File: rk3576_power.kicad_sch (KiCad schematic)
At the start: 30 parts, among them U27 RK3576

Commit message: Add files via upload
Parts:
- C63: renamed from C398; value 100n -> 1u
- C64: renamed from C259; value 100n -> 1u
- C65: renamed from C266; value 100n -> 1u
- C74: renamed from C419; value 100n -> 1u
- C75: renamed from C408; value 100n -> 1u
- C76: renamed from C409; value 100n -> 1u
- C83: renamed from C423; value 100n -> 1u
- C84: renamed from C424; value 100n -> 1u
- C85: renamed from C417; value 100n -> 1u
- renumbered C407 to C60, C402 to C61, C399 to C62, C267 to C66, C268 to C67, C270 to C68, C271 to C69, C272 to C70, C273 to C71, C416 to C72, C418 to C73, C410 to C77, C411 to C78, C412 to C79, C413 to C80, C414 to C81, C415 to C82, C420 to C86, C421 to C87, C422 to C88, U27 to U2

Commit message: SBC Board V0.2
The SBC schematics before footprint and part number check
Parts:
- U3: renamed from U2; footprint (none) -> easyeda2kicad:FCCSP-698_L17.2-W16.1-TL_RK3576
- renumbered C60 to C67, C61 to C68, C62 to C69, C63 to C70, C64 to C71, C65 to C72, C66 to C73, C67 to C74, C68 to C75, C69 to C76, C70 to C77, C71 to C78, C72 to C79, C73 to C80, C74 to C81, C75 to C82, C76 to C83, C77 to C84, C78 to C85, C79 to C86, C80 to C87, C81 to C88, C82 to C89, C83 to C90, C84 to C91, C85 to C92, C86 to C93, C87 to C94, C88 to C95

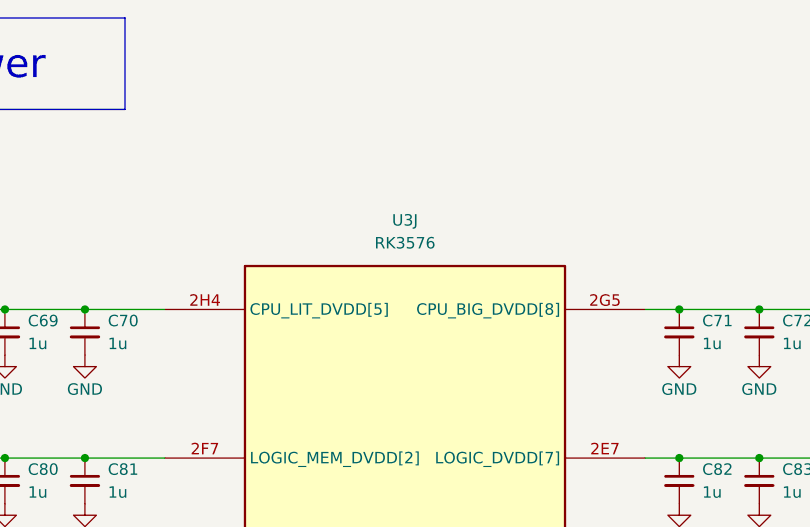
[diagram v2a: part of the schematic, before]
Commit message: SBCv0.3
there is no big thing update just some LCSC & Mouser parts
and Big problem deleted alot of component values (:
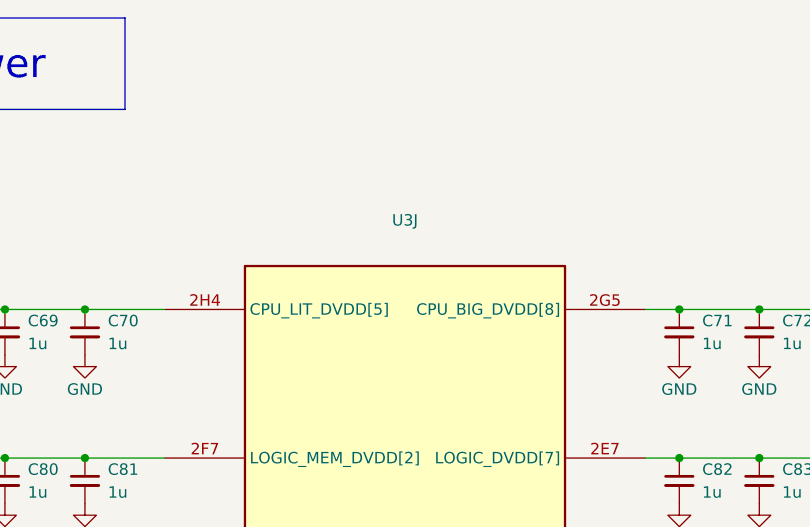
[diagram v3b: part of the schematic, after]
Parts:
- C67, C77, C78, C79, C86, C87, C95: footprint Capacitor_SMD:C_0402_1005Metric_Pad0.74x0.62mm_HandSolder -> Capacitor_SMD:C_0603_1608Metric; LCSC Part (none) -> C19702; Mouser Part (none) -> 187-CL10A106KP8NNNC
- C68, C69, C70, C71, C72, C73, C74, C75, C76, C80, C81, C82, C83, C84, C85, C88, C89, C90, C91, C92, C93, C94: footprint Capacitor_SMD:C_0402_1005Metric_Pad0.74x0.62mm_HandSolder -> Capacitor_SMD:C_0201_0603Metric_Pad0.64x0.40mm_HandSolder; LCSC Part (none) -> C5209398; Mouser Part (none) -> CL03A105KP3NSNC
- U3: value RK3576 -> (none); LCSC Part (none) -> (polyline

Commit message: SBCv0.4
add LCSC & Mouser parts 
and solve the deleted value in the past version
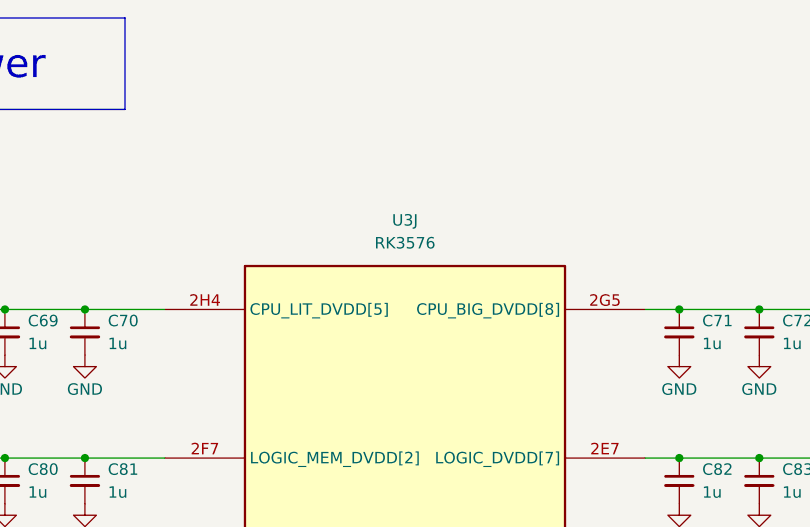
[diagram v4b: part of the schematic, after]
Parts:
- U3: value (none) -> RK3576; LCSC Part (polyline -> C42388007
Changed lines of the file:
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@@
 			)
 		)
-		(property "Value" ""
+		(property "Value" "RK3576"
 			(at 92.71 37.084 0)
 			(show_name no)
@@
 			)
 		)
-		(property "LCSC Part" "(polyline"
+		(property "LCSC Part" "C42388007"
 			(at 92.71 67.31 0)
 			(hide yes)
